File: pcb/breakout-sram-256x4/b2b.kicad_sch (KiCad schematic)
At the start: 10 parts, among them J1 DF40C-100DS-0.4V51, J10 DF40C-40DP-0.4V51, J2 DF40C-100DS-0.4V51, J3 DF40C-100DS-0.4V51, J4 DF40C-100DS-0.4V51, J5 DF40C-100DP-0.4V51, J6 DF40C-100DP-0.4V51, J7 DF40C-100DP-0.4V51, J8 DF40C-100DP-0.4V51, J9 DF40C-40DS-0.4V51

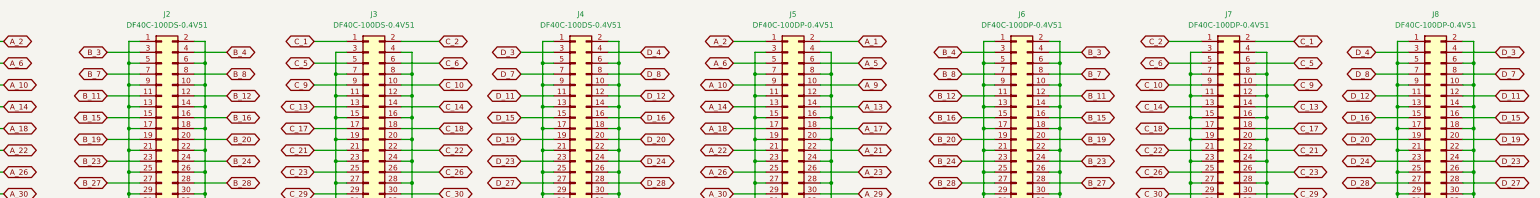
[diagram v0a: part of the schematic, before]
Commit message: [sram_4x][pcb] do not use nc from ice40
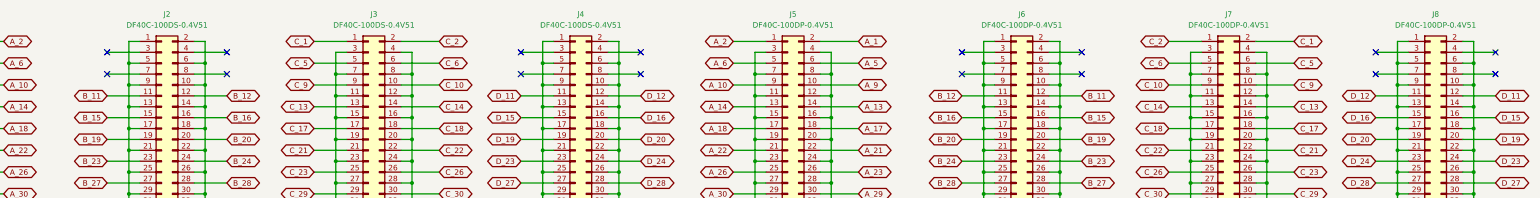
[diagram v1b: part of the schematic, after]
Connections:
- net B_3: no longer names the net of J2.3
- net B_3: no longer J6.4
- net B_4: no longer names the net of J2.4
- net B_4: no longer J6.3
- net B_7: no longer names the net of J2.7
- net B_7: no longer J6.8
- net B_8: no longer names the net of J2.8
- net B_8: no longer J6.7
- net D_3: no longer names the net of J8.4
- net D_3: no longer J4.3
- net D_4: no longer names the net of J8.3
- net D_4: no longer J4.4
- net D_7: no longer names the net of J8.8
- net D_7: no longer J4.7
- net D_8: no longer names the net of J8.7
- net D_8: no longer J4.8
- no-connect marks 40 -> 56

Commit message: [adc][sram] fix part numbers for plugs
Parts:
- J10: Digi-Key Part Number H11625CT-ND -> H11624CT-ND
- J5, J6, J7, J8: Digi-Key Part Number H11615CT-ND -> H11614CT-ND; LCSC Part # C597931 -> C531031
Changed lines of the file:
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@@
 			)
 		)
-		(property "Digi-Key Part Number" "H11615CT-ND"
+		(property "Digi-Key Part Number" "H11614CT-ND"
 			(at 240.03 87.63 0)
 			(effects
@@
 			)
 		)
-		(property "LCSC Part #" "C597931"
+		(property "LCSC Part #" "C531031"
 			(at 240.03 87.63 0)
 			(effects
@@
 			)
 		)
-		(property "Digi-Key Part Number" "H11615CT-ND"
+		(property "Digi-Key Part Number" "H11614CT-ND"
 			(at 293.37 87.63 0)
 			(effects
@@
 			)
 		)
-		(property "LCSC Part #" "C597931"
+		(property "LCSC Part #" "C531031"
 			(at 293.37 87.63 0)
 			(effects
@@
 			)
 		)
-		(property "Digi-Key Part Number" "H11615CT-ND"
+		(property "Digi-Key Part Number" "H11614CT-ND"
 			(at 341.63 87.63 0)
 			(effects
@@
 			)
 		)
-		(property "LCSC Part #" "C597931"
+		(property "LCSC Part #" "C531031"
 			(at 341.63 87.63 0)
 			(effects
@@
 			)
 		)
-		(property "Digi-Key Part Number" "H11625CT-ND"
+		(property "Digi-Key Part Number" "H11624CT-ND"
 			(at 321.31 198.12 0)
 			(effects
@@
 			)
 		)
-		(property "Digi-Key Part Number" "H11615CT-ND"
+		(property "Digi-Key Part Number" "H11614CT-ND"
 			(at 389.89 87.63 0)
 			(effects
@@
 			)
 		)
-		(property "LCSC Part #" "C597931"
+		(property "LCSC Part #" "C531031"
 			(at 389.89 87.63 0)
 			(effects

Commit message: [sram_4x][pcb] fix A_25 net label
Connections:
- net A_23 renamed A_25
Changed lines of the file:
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@@
 (kicad_sch
-	(version 20231120)
+	(version 20250114)
 	(generator "eeschema")
-	(generator_version "8.0")
+	(generator_version "9.0")
 	(paper "USLedger")
 	(junction
@@
 		)
 	)
-	(global_label "A_23"
+	(global_label "A_25"
 		(shape bidirectional)
 		(at 256.54 57.15 0)
@@
 		)
 	)
-	(global_label "A_23"
+	(global_label "A_25"
 		(shape bidirectional)
 		(at 27.94 57.15 180)

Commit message: [sram_4x][pcb] fix C_25 net label
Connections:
- net C_23 renamed C_25
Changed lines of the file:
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@@
 		)
 	)
-	(global_label "C_23"
+	(global_label "C_25"
 		(shape bidirectional)
 		(at 358.14 57.15 0)
@@
 		)
 		(property "Intersheetrefs" "${INTERSHEET_REFS}"
-			(at 366.7117 57.15 0)
+			(at 366.8931 57.15 0)
 			(effects
 				(font
@@
 		)
 	)
-	(global_label "C_23"
+	(global_label "C_25"
 		(shape bidirectional)
 		(at 129.54 57.15 180)
@@
 		)
 		(property "Intersheetrefs" "${INTERSHEET_REFS}"
-			(at 120.9683 57.15 0)
+			(at 120.7869 57.15 0)
 			(effects
 				(font
